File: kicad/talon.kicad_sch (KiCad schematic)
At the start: 39 parts, among them J1 JST connector, SW1 SW_Push, SW10 SW_Push, SW11 SW_Push, SW12 SW_Push, SW13 SW_Push, SW14 SW_Push, SW15 SW_Push, SW16 SW_Push, SW17 SW_Push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

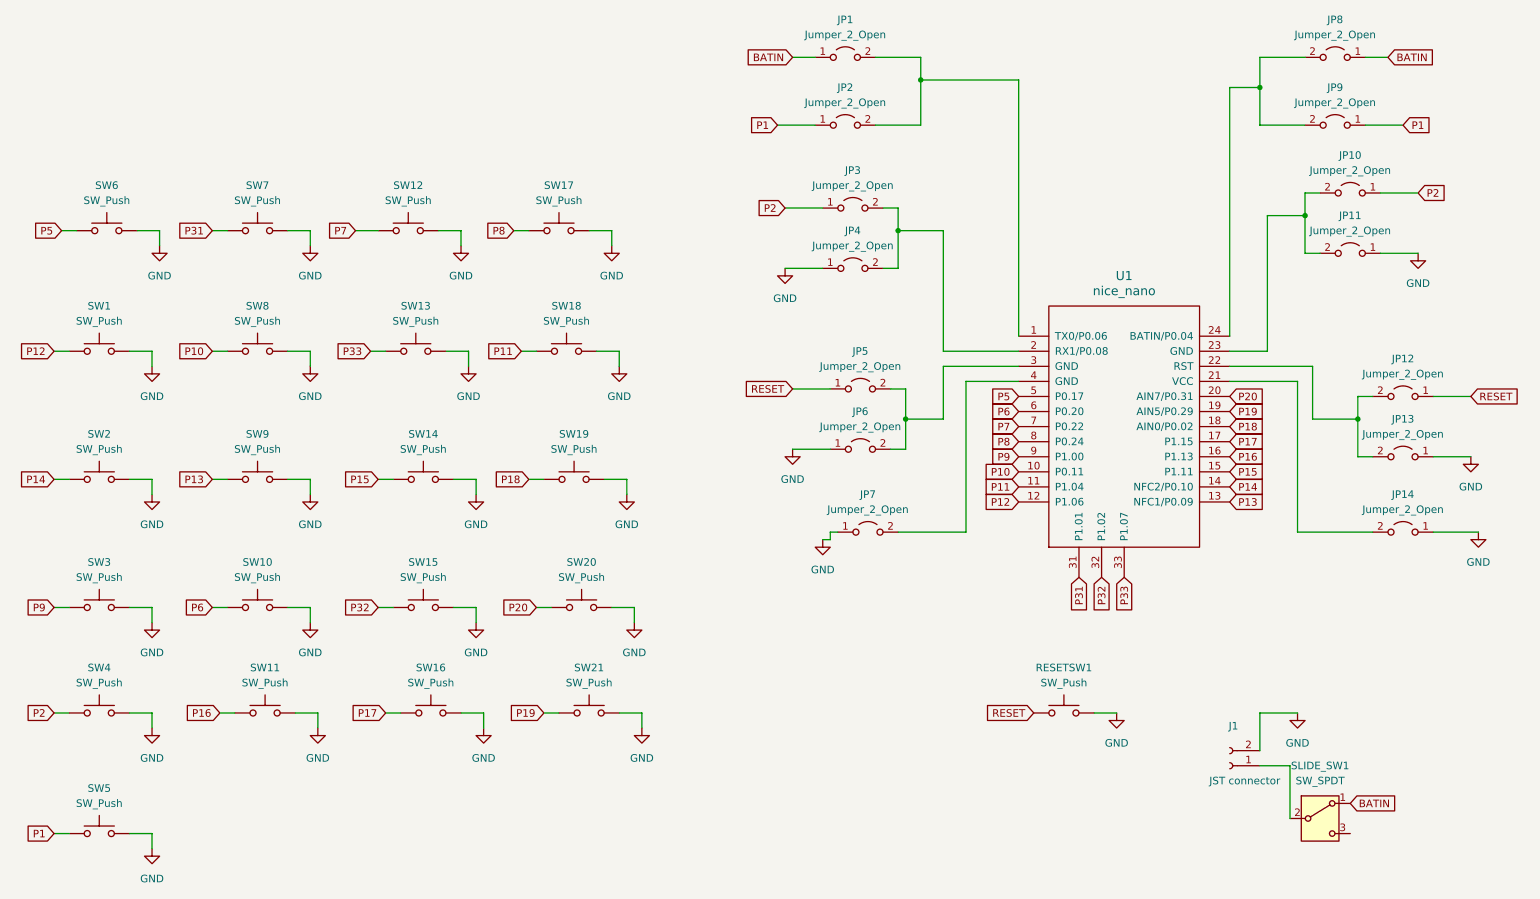
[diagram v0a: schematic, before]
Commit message: working on routing
Battery connection gnd is disconnected from fill.
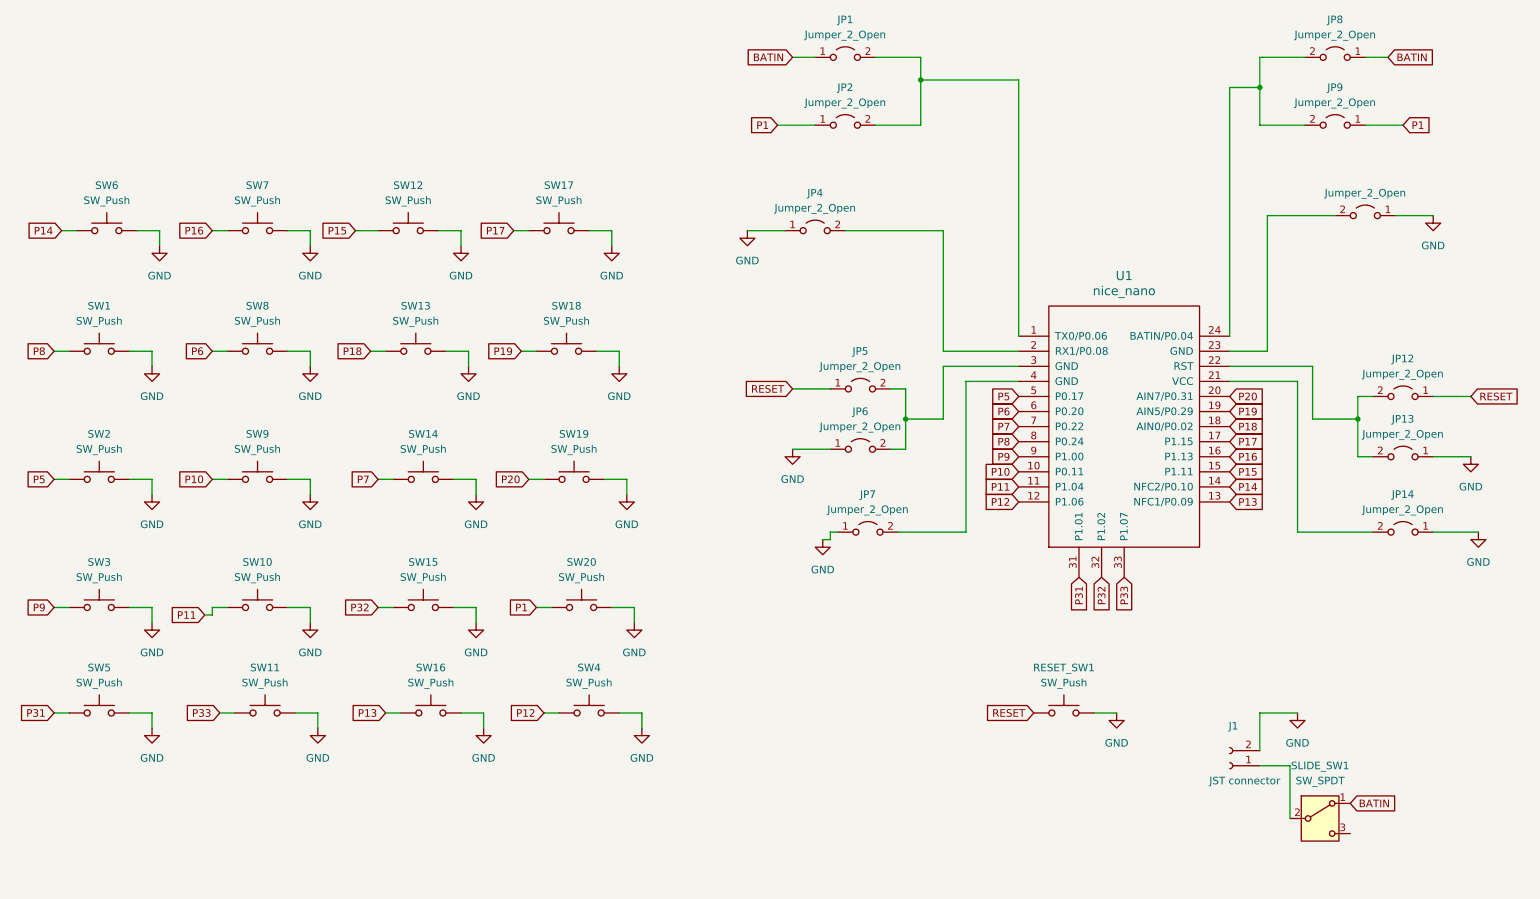
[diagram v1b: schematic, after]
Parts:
- removed JP10, JP3: Jumper_2_Open, footprints:Jumper_Open_0.5mm, symbol Jumper:Jumper_2_Open
- removed SW4: SW_Push, footprints:Kailh_socket_MX_reversible_1U, symbol Switch:SW_Push
- SW10, SW11, SW15, SW3, SW5, SW7: footprint footprints:Kailh_socket_MX_reversible_1_25U -> footprints:Kailh_socket_MX_reversible_1U
- SW16: footprint footprints:Kailh_socket_MX_reversible_1_5U -> footprints:Kailh_socket_MX_reversible_1U
- SW18, SW19, SW8: footprint footprints:Kailh_socket_MX_reversible_1U -> footprints:Kailh_socket_MX_reversible_1_25U
- SW20: footprint footprints:Kailh_socket_MX_reversible_1_5U -> footprints:Kailh_socket_MX_reversible_1_25U
- SW4: renamed from SW21; footprint footprints:Kailh_socket_MX_reversible_1_5U -> footprints:Kailh_socket_MX_reversible_1U
- renumbered RESETSW1 to RESET_SW1
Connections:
- net P1: now also SW20.1; no longer SW5.1
- net P10: now also SW9.1; no longer SW8.1
- net P11: now also SW10.1; no longer SW18.1
- net P12: now also SW4.1; no longer SW1.1
- net P13: now also SW16.1; no longer SW9.1
- net P14: now also SW6.1; no longer SW2.1
- net P15: now also SW12.1; no longer SW14.1
- net P16: now also SW7.1; no longer SW11.1
- net P17: now also SW17.1; no longer SW16.1
- net P18: now also SW13.1; no longer SW19.1
- net P19: now also SW18.1; no longer SW4.1
- net P20: now also SW19.1; no longer SW20.1
- net P31: now also SW5.1; no longer SW7.1
- net P33: now also SW11.1; no longer SW13.1
- net P5: now also SW2.1; no longer SW6.1
- net P6: now also SW8.1; no longer SW10.1
- net P7: now also SW14.1; no longer SW12.1
- net P8: now also SW1.1; no longer SW17.1
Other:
- moved on the sheet: JP4, SW5
